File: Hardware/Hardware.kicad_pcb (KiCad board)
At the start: 2 copper layers, 108 x 61.2 mm, 66 parts, among them J1 LINEIN, J2 MICIN, J3 Raspberry_Pi_2_3, J4 LOUT, J5 HPOUT, SW1 JS5208, U1 MCP3004, U2 WM8731SEDS

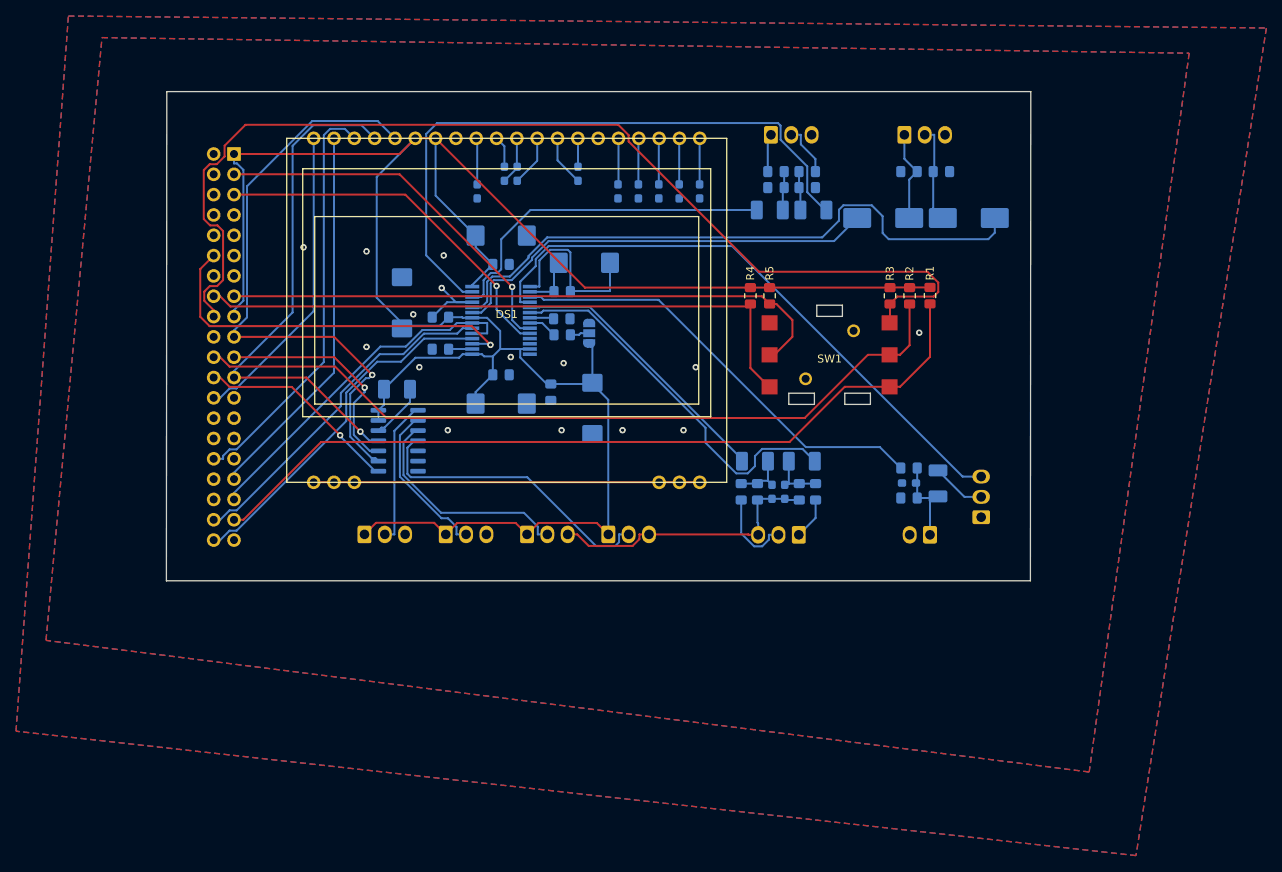
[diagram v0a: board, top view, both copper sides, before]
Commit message: Moved I2C lines, added mounting holes, took renders.
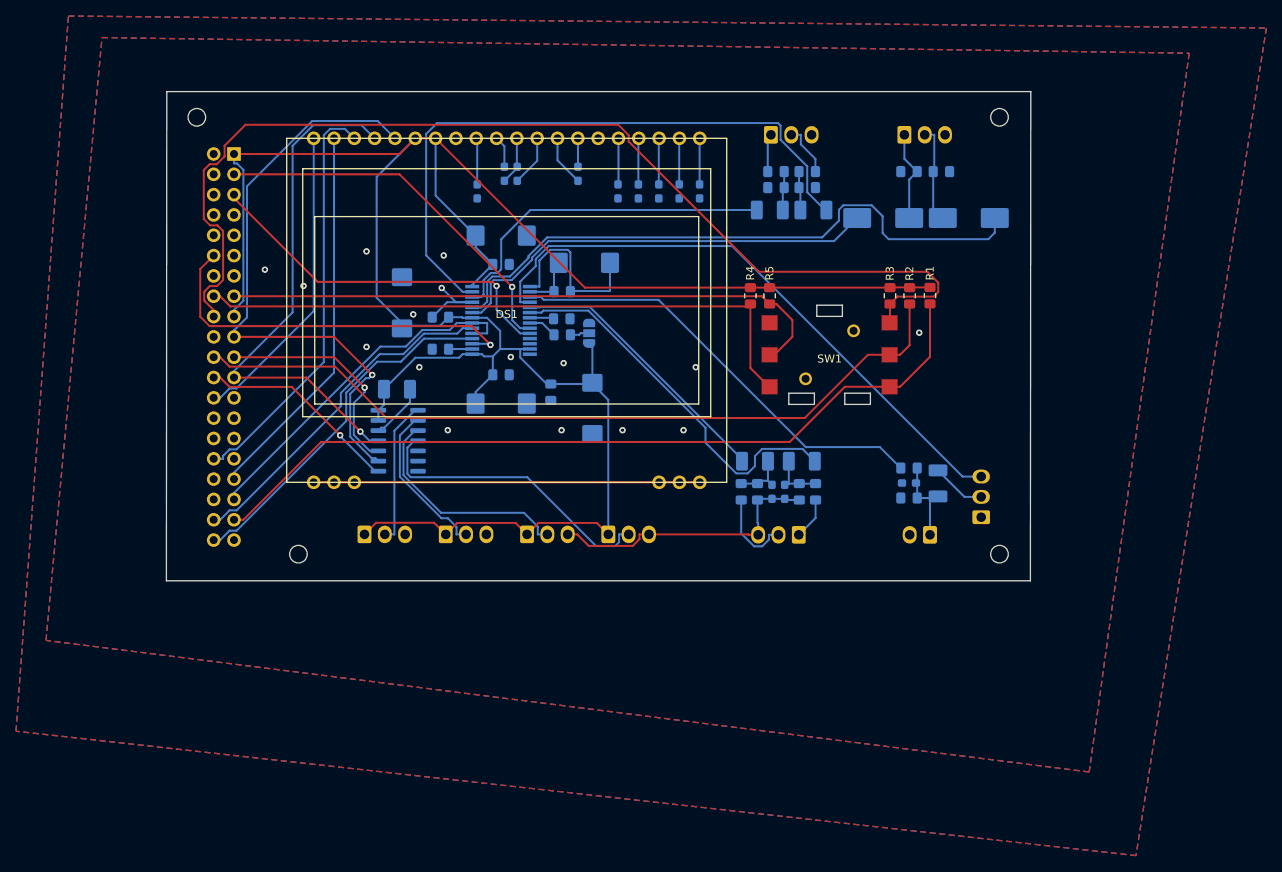
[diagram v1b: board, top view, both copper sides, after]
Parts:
- added REF**: MountingHole_2.2mm_M2, MountingHole:MountingHole_2.2mm_M2, F.Cu at (172.1, 29.2)
- added REF**: MountingHole_2.2mm_M2, MountingHole:MountingHole_2.2mm_M2, F.Cu at (172.1, 83.8)
- added REF**: MountingHole_2.2mm_M2, MountingHole:MountingHole_2.2mm_M2, F.Cu at (84.5, 83.8)
- added REF**: MountingHole_2.2mm_M2, MountingHole:MountingHole_2.2mm_M2, F.Cu at (71.8, 29.2)
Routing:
- net GNDD: vias 12 -> 13
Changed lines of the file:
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@@
     (thickness 1.6)
     (drawings 25)
-    (tracks 494)
+    (tracks 497)
     (zones 0)
-    (modules 66)
+    (modules 70)
     (nets 81)
   )
   (page A4)
   (layers
-    (0 F.Cu signal hide)
-    (31 B.Cu signal hide)
+    (0 F.Cu signal)
+    (31 B.Cu signal)
     (32 B.Adhes user)
     (33 F.Adhes user)
@@
     (add_net "Net-(U2-Pad26)")
   )
+  (module MountingHole:MountingHole_2.2mm_M2 (layer F.Cu)
+    (at 172.085 29.21)
+    (descr "Mounting Hole 2.2mm, no annular, M2")
+    (tags "mounting hole 2.2mm no annular m2")
+    (attr virtual)
+    (fp_text reference REF** (at 0 -3.2) (layer F.SilkS) hide
+      (effects (font (size 1 1) (thickness 0.15)))
+    )
+    (fp_text value MountingHole_2.2mm_M2 (at 0 3.2) (layer F.Fab)
+      (effects (font (size 1 1) (thickness 0.15)))
+    )
+    (fp_circle (center 0 0) (end 2.45 0) (layer F.CrtYd) (width 0.05))
+    (fp_circle (center 0 0) (end 2.2 0) (layer Cmts.User) (width 0.15))
+    (fp_text user %R (at 0.3 0) (layer F.Fab)
+      (effects (font (size 1 1) (thickness 0.15)))
+    )
+    (pad 1 np_thru_hole circle (at 0 0) (size 2.2 2.2) (drill 2.2) (layers *.Cu *.Mask))
+  )
+  (module MountingHole:MountingHole_2.2mm_M2 (layer F.Cu)
+    (at 172.085 83.82)
+    (descr "Mounting Hole 2.2mm, no annular, M2")
+    (tags "mounting hole 2.2mm no annular m2")
+    (attr virtual)
+    (fp_text reference REF** (at 0 -3.2) (layer F.SilkS) hide
+      (effects (font (size 1 1) (thickness 0.15)))
+    )
+    (fp_text value MountingHole_2.2mm_M2 (at 0 3.2) (layer F.Fab)
+      (effects (font (size 1 1) (thickness 0.15)))
+    )
+    (fp_circle (center 0 0) (end 2.45 0) (layer F.CrtYd) (width 0.05))
+    (fp_circle (center 0 0) (end 2.2 0) (layer Cmts.User) (width 0.15))
+    (fp_text user %R (at 0.3 0) (layer F.Fab)
+      (effects (font (size 1 1) (thickness 0.15)))
+    )
+    (pad 1 np_thru_hole circle (at 0 0) (size 2.2 2.2) (drill 2.2) (layers *.Cu *.Mask))
+  )
+  (module MountingHole:MountingHole_2.2mm_M2 (layer F.Cu)
+    (at 84.455 83.82)
+    (descr "Mounting Hole 2.2mm, no annular, M2")
+    (tags "mounting hole 2.2mm no annular m2")
+    (attr virtual)
+    (fp_text reference REF** (at 0 -3.2) (layer F.SilkS) hide
+      (effects (font (size 1 1) (thickness 0.15)))
+    )
+    (fp_text value MountingHole_2.2mm_M2 (at 0 3.2) (layer F.Fab)
+      (effects (font (size 1 1) (thickness 0.15)))
+    )
+    (fp_circle (center 0 0) (end 2.45 0) (layer F.CrtYd) (width 0.05))
+    (fp_circle (center 0 0) (end 2.2 0) (layer Cmts.User) (width 0.15))
+    (fp_text user %R (at 0.3 0) (layer F.Fab)
+      (effects (font (size 1 1) (thickness 0.15)))
+    )
+    (pad 1 np_thru_hole circle (at 0 0) (size 2.2 2.2) (drill 2.2) (layers *.Cu *.Mask))
+  )
+  (module MountingHole:MountingHole_2.2mm_M2 (layer F.Cu)
+    (at 71.755 29.21)
+    (descr "Mounting Hole 2.2mm, no annular, M2")
+    (tags "mounting hole 2.2mm no annular m2")
+    (attr virtual)
+    (fp_text reference REF** (at 0 -3.2) (layer F.SilkS) hide
+      (effects (font (size 1 1) (thickness 0.15)))
+    )
+    (fp_text value MountingHole_2.2mm_M2 (at 0 3.2) (layer F.Fab)
+      (effects (font (size 1 1) (thickness 0.15)))
+    )
+    (fp_circle (center 0 0) (end 2.45 0) (layer F.CrtYd) (width 0.05))
+    (fp_circle (center 0 0) (end 2.2 0) (layer Cmts.User) (width 0.15))
+    (fp_text user %R (at 0.3 0) (layer F.Fab)
+      (effects (font (size 1 1) (thickness 0.15)))
+    )
+    (pad 1 np_thru_hole circle (at 0 0) (size 2.2 2.2) (drill 2.2) (layers *.Cu *.Mask))
+  )
   (module signl:signl_logo (layer B.Cu)
     (at 164.846 55.372 180)
@@
     (pad 21 thru_hole circle (at 24.13 -21.5) (size 1.7 1.7) (drill 1) (layers *.Cu *.Mask)
       (net 7 "Net-(C6-Pad1)"))
+    (model "${KIPRJMOD}/signl.pretty/ea dogm128.wrl"
+      (offset (xyz -17 -25.5 -46.5))
+      (scale (xyz 0.39 0.39 0.4))
+      (rotate (xyz 0 0 0))
+    )
   )
   (module Resistor_SMD:R_0805_2012Metric_Pad1.15x1.40mm_HandSolder (layer B.Cu)
@@
   (via (at 92.964 45.974) (size 0.8) (drill 0.4) (layers F.Cu B.Cu) (net 2))
   (via (at 134.112 60.452) (size 0.8) (drill 0.4) (layers F.Cu B.Cu) (net 2))
-  (via (at 85.09 45.466) (size 0.8) (drill 0.4) (layers F.Cu B.Cu) (net 2))
+  (via (at 85.09 50.292) (size 0.8) (drill 0.4) (layers F.Cu B.Cu) (net 2))
   (via (at 102.616 46.482) (size 0.8) (drill 0.4) (layers F.Cu B.Cu) (net 2))
+  (via (at 80.264 48.26) (size 0.8) (drill 0.4) (layers F.Cu B.Cu) (net 2))
   (segment (start 124.46 31.84) (end 124.46 37.54) (width 0.25) (layer B.Cu) (net 3) (status 30))
   (segment (start 124.46 37.54) (end 124.4 37.6) (width 0.25) (layer B.Cu) (net 3) (status 30))
@@
   (segment (start 160.875 50.475) (end 158.425 50.475) (width 0.25) (layer F.Cu) (net 10) (status 30))
   (segment (start 158.425 50.475) (end 158.4 50.5) (width 0.25) (layer F.Cu) (net 10) (status 30))
-  (segment (start 143.35 50.5) (end 158.4 50.5) (width 0.25) (layer F.Cu) (net 10) (status 30))
   (segment (start 106.18 54.275) (end 108.036411 54.275) (width 0.25) (layer B.Cu) (net 10) (status 10))
   (segment (start 108.036411 54.275) (end 109.6728 55.911389) (width 0.25) (layer B.Cu) (net 10))
@@
   (segment (start 99.06 31.84) (end 94.234 36.666) (width 0.25) (layer B.Cu) (net 10))
   (segment (start 94.234 36.666) (end 94.234 51.7628) (width 0.25) (layer B.Cu) (net 10))
+  (segment (start 143.35 50.5) (end 158.4 50.5) (width 0.25) (layer F.Cu) (net 10) (status 30))
   (via (at 110.998 59.182) (size 0.8) (drill 0.4) (layers F.Cu B.Cu) (net 11))
   (segment (start 113.38 50.375) (end 114.5803 50.375) (width 0.25) (layer B.Cu) (net 11) (status 10))
@@
   (segment (start 113.38 55.575) (end 112.1797 55.575) (width 0.25) (layer B.Cu) (net 38) (status 10))
   (via (at 111.1725 50.4139) (size 0.8) (layers F.Cu B.Cu) (net 38))
-  (segment (start 97.808 38.88) (end 109.22 50.292) (width 0.25) (layer F.Cu) (net 39))
   (segment (start 109.22 53.2653) (end 109.22 50.292) (width 0.25) (layer B.Cu) (net 39))
   (segment (start 113.38 56.225) (end 112.1797 56.225) (width 0.25) (layer B.Cu) (net 39) (status 10))
-  (segment (start 76.4 38.88) (end 97.808 38.88) (width 0.25) (layer F.Cu) (net 39) (status 10))
   (via (at 109.22 50.292) (size 0.8) (drill 0.4) (layers F.Cu B.Cu) (net 39))
   (segment (start 112.1797 56.225) (end 109.22 53.2653) (width 0.25) (layer B.Cu) (net 39))
+  (segment (start 108.712 49.784) (end 109.22 50.292) (width 0.25) (layer F.Cu) (net 39))
+  (segment (start 86.868 49.784) (end 108.712 49.784) (width 0.25) (layer F.Cu) (net 39))
+  (segment (start 76.4 39.316) (end 86.868 49.784) (width 0.25) (layer F.Cu) (net 39))
+  (segment (start 76.4 38.88) (end 76.4 39.316) (width 0.25) (layer F.Cu) (net 39))
   (via (at 108.457998 57.658) (size 0.8) (drill 0.4) (layers F.Cu B.Cu) (net 40))
   (segment (start 73.3508 55.3171) (end 106.117098 55.3171) (width 0.25) (layer F.Cu) (net 40))

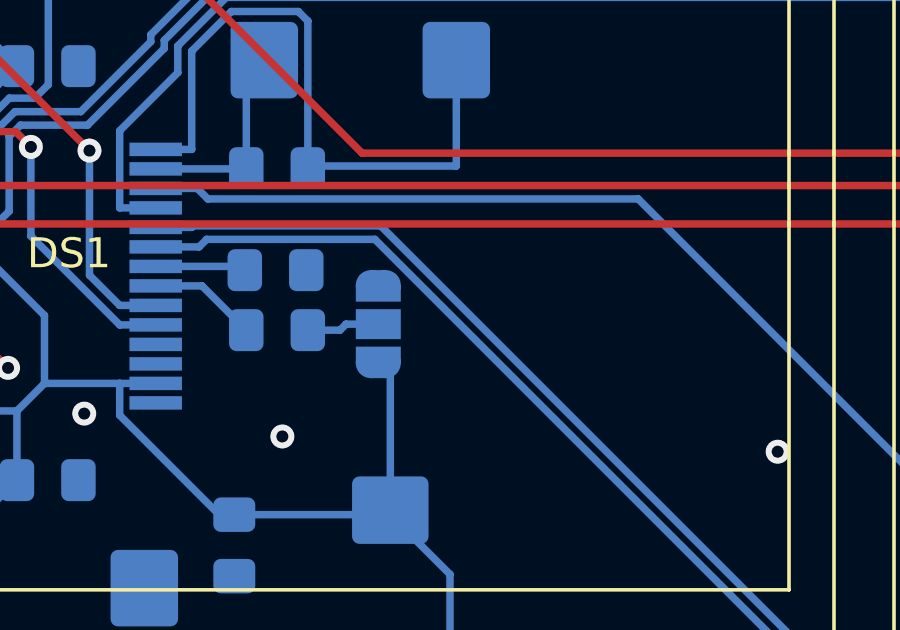
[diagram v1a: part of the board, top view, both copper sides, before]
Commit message: Added JLC serial code, created gerbers of main PCB.
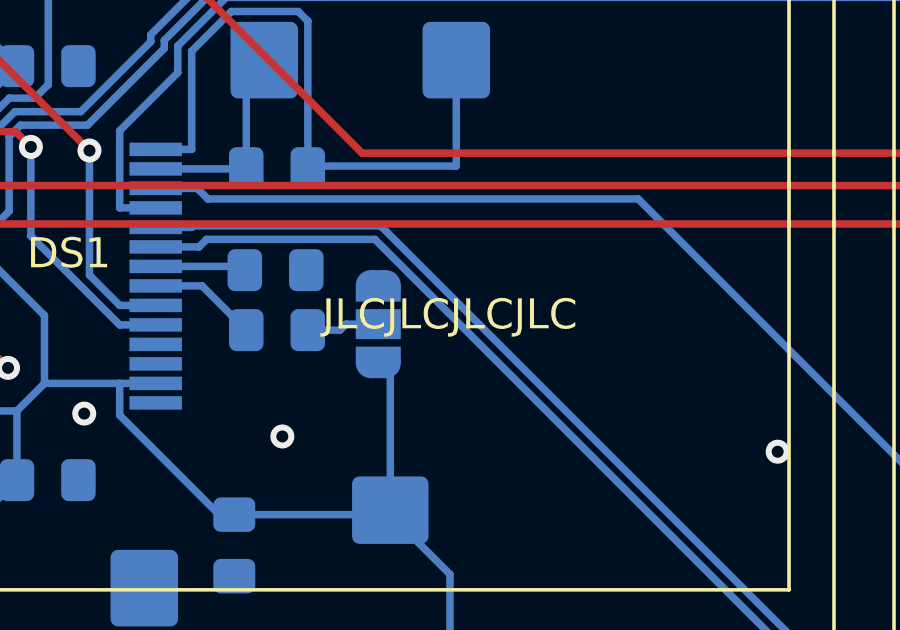
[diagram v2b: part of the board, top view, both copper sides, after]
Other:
- board text added: "JLCJLCJLCJLC"
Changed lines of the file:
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@@
   (general
     (thickness 1.6)
-    (drawings 25)
+    (drawings 26)
     (tracks 497)
     (zones 0)
@@
     )
   )
+  (gr_text JLCJLCJLCJLC (at 123.19 55.88) (layer F.SilkS)
+    (effects (font (size 1 1) (thickness 0.15)))
+  )
   (gr_text "Rev 1.\nAlexander Strachan\nRobert Norris\nSimon Ridley" (at 164.592 65.786) (layer B.SilkS)

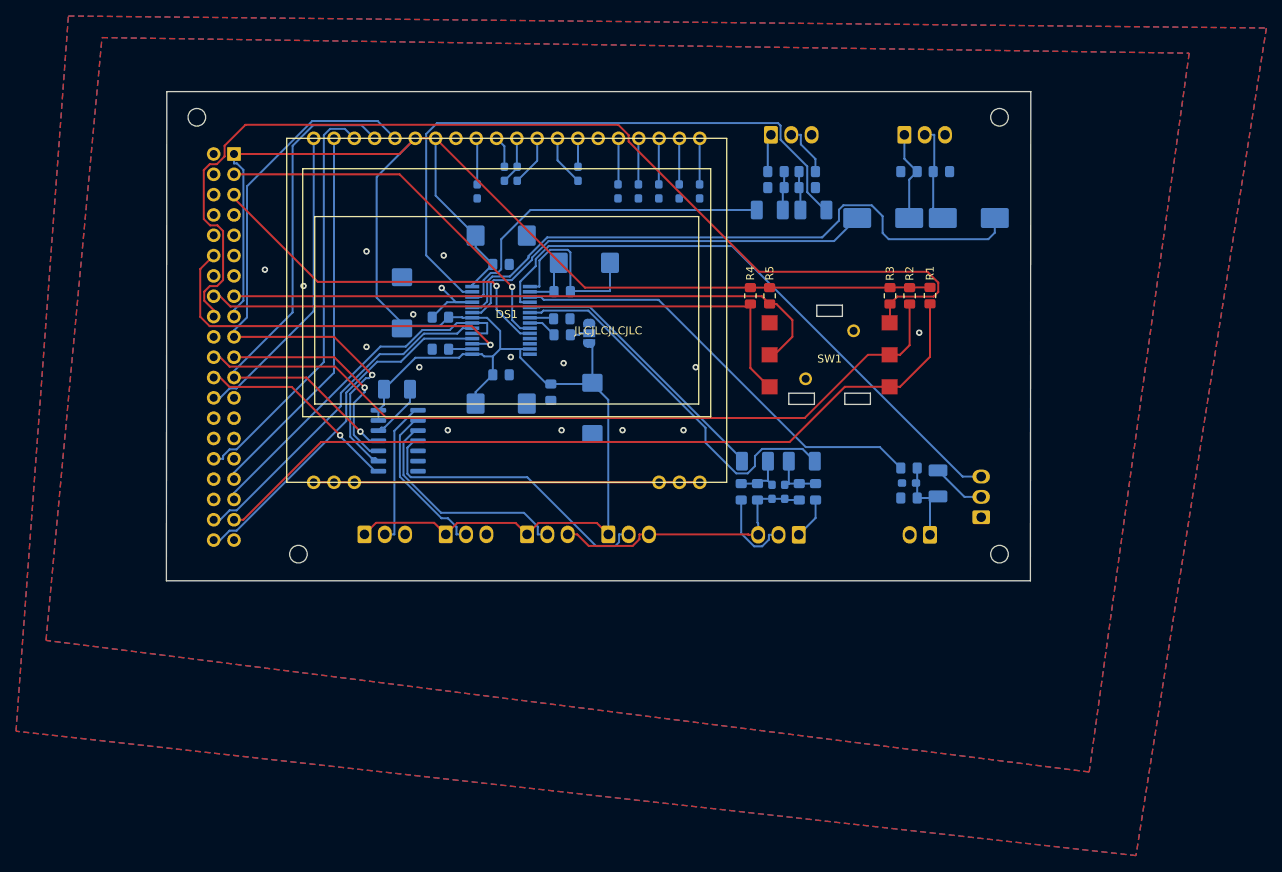
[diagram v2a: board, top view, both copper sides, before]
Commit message: Added external oscillator to Schematic and PCB. Plotted outputs.
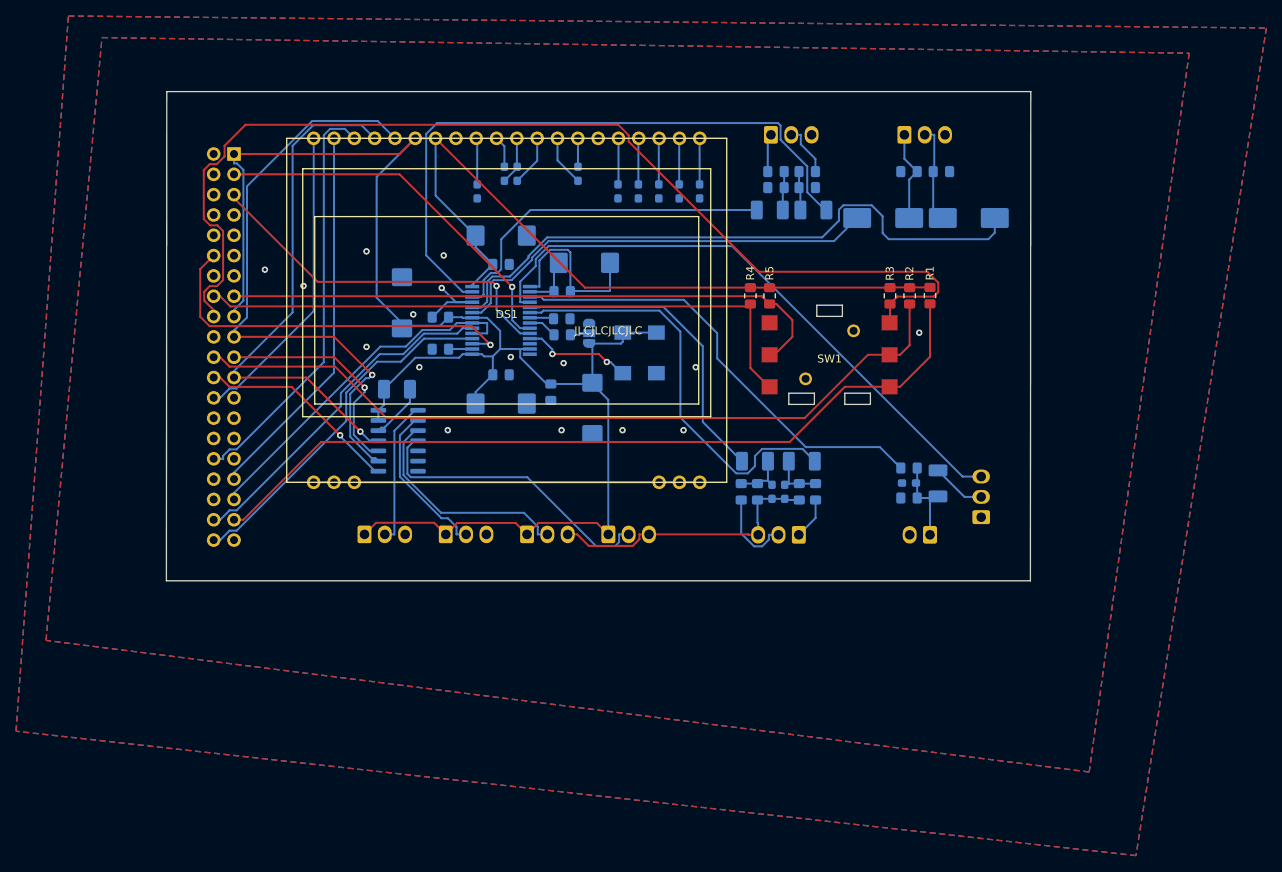
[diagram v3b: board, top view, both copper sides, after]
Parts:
- removed G***: LOGO, signl:signl_logo
- removed REF** (x4): MountingHole_2.2mm_M2, MountingHole:MountingHole_2.2mm_M2
- added Y1: CO4305-12.000, signl:CO4305-12.000, B.Cu at (127.1, 58.7)
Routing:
- net Net-(U2-Pad25): track 0.00 -> 13.7 mm, vias 0 -> 2
- net +3V3: track 284.2 -> 293.9 mm
- net /RLINEIN: track 34.7 -> 40.1 mm
- net /LLINEIN: track 47.9 -> 53.1 mm
- net /MICBIAS: track 55.2 -> 57.1 mm
